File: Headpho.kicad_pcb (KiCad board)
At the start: 2 copper layers, 20 x 106.7 mm, 39 parts, among them IC1 NJM4556AD, IC2 NJM4556AD, J1 IN L, J2 IN R, J3 Eurorack_Power_10pin_Unshroud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, J4 LINE OUT L, J5 OUT LR, J6 LINE OUT R, U1 LME49720, U2 LME49720

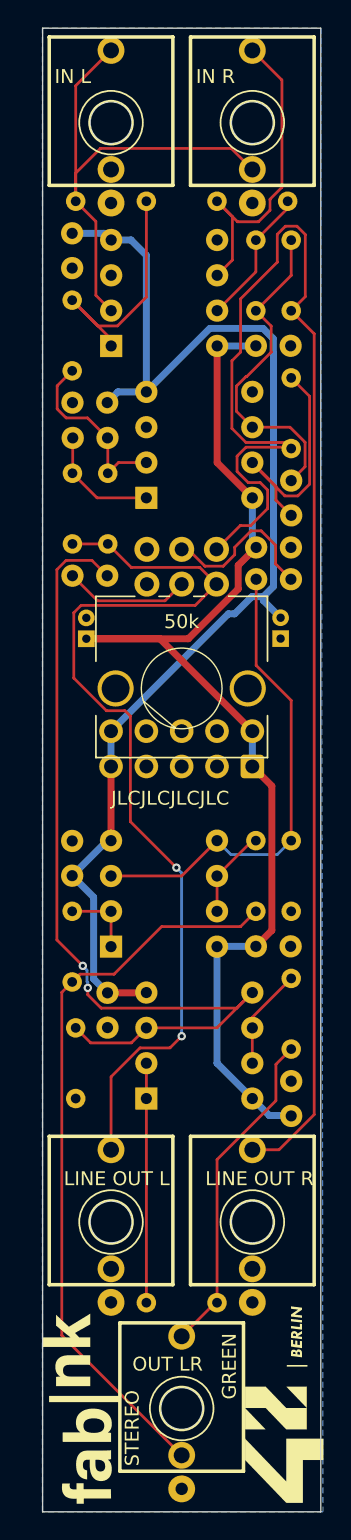
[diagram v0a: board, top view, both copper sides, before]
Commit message: added BuildNotes.md. Removed production folder
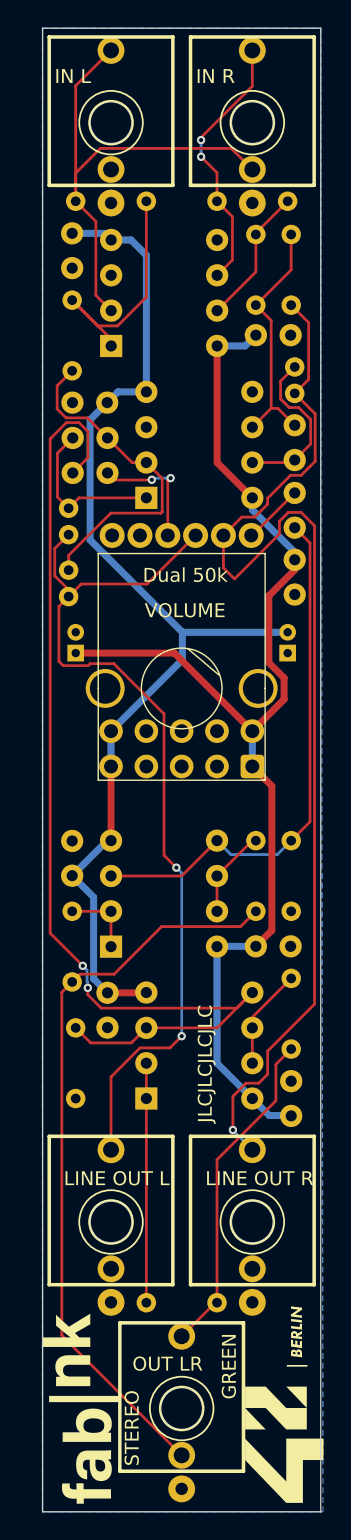
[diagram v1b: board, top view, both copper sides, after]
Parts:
- POT1: footprint PCM_4ms_Potentiometer:Potentiometer_Alps_RK09L_Double_Vertical -> Library:Dual_9mm_Potentiometer_50K_RK1114GH
- R5, R7, R8: footprint Resistor_THT:R_Axial_DIN0204_L3.6mm_D1.6mm_P5.08mm_Horizontal -> Resistor_THT:R_Axial_DIN0204_L3.6mm_D1.6mm_P1.90mm_Vertical
- moved C13 7.81 mm to (55.6, 82.8), turned to 180 degrees
- moved R5 7.51 mm to (52.8, 89.8)
- moved C14 6.21 mm to (69.1, 84.2), turned to -90 degrees
- moved C12 3.99 mm to (69.1, 79.4)
- moved C5 2.91 mm to (69.1, 89.0), turned to -90 degrees
- moved R7 2.53 mm to (52.8, 85.3)
- moved C1 1.28 mm to (53.3, 95.7)
- moved C2 1.16 mm to (68.6, 95.7)
- moved R8 0.83 mm to (69.1, 75.2)
- moved C3 0.77 mm to (66.3, 72.9)
- moved R4 0.40 mm to (66.3, 65.6)
- moved R6 0.40 mm to (68.8, 65.6)
- turned POT1 to 180 degrees
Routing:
- net Net-(J6-SIG): track 106.8 -> 82.4 mm, vias 0 -> 1
- net Net-(IC1-A_+INPUT): track 63.2 -> 75.3 mm
- net Net-(U2A--): track 13.3 -> 24.3 mm
- net -12V: track 90.1 -> 79.5 mm
- net Net-(POT1B-Center): track 11.9 -> 4.39 mm
- net Net-(C12-Pad2): track 18.6 -> 12.0 mm
- net Net-(U2B--): track 23.9 -> 18.3 mm
- net Net-(J2-SIG): track 23.7 -> 19.1 mm, vias 0 -> 2
- net Net-(IC2-A_+INPUT): track 34.7 -> 38.4 mm
- net Net-(C11-Pad2): track 8.59 -> 11.7 mm
- net Net-(J4-SIG): track 68.6 -> 65.6 mm
- net +12V: track 83.7 -> 85.0 mm
- net Net-(POT1A-Center): track 9.10 -> 9.01 mm, vias 0 -> 2

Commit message: v1.1 ready for final check
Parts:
- C1, C2: footprint Capacitor_THT:CP_Radial_D4.0mm_P1.50mm -> Capacitor_THT:CP_Radial_D4.0mm_P2.00mm
- IC1, U2: moved to F.Cu
- R1, R10, R2, R3, R4, R6, R9: footprint Resistor_THT:R_Axial_DIN0204_L3.6mm_D1.6mm_P5.08mm_Horizontal -> Resistor_THT:R_Axial_DIN0204_L3.6mm_D1.6mm_P1.90mm_Vertical
- R11, R12, R13, R14: value 1 -> 1Ω; footprint Resistor_THT:R_Axial_DIN0204_L3.6mm_D1.6mm_P5.08mm_Horizontal -> Resistor_THT:R_Axial_DIN0204_L3.6mm_D1.6mm_P1.90mm_Vertical
- moved R6 35.9 mm to (52.8, 97.8)
- moved R8 31.7 mm to (52.8, 102.3)
- moved C14 27.9 mm to (52.8, 106.9)
- moved C13 27.5 mm to (69.1, 106.8), turned to -90 degrees
- moved R7 23.4 mm to (69.1, 102.2)
- moved R9 20.2 mm to (65.3, 111.5), turned to 0 degrees
- moved R5 18.1 mm to (69.1, 97.6)
- moved R11 17.6 mm to (67.3, 127.2), turned to -90 degrees
- moved R1 16.7 mm to (53.1, 80.0)
- moved J3 16.4 mm to (66.0, 87.5)
- moved R12 16.4 mm to (54.6, 127.2)
- moved C11 16.2 mm to (64.6, 66.8)
- moved C6 15.7 mm to (68.3, 64.3), turned to -90 degrees
- moved C12 15.6 mm to (59.8, 66.8), turned to 180 degrees
- moved C2 15.3 mm to (53.3, 94.7)
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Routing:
- net Net-(IC1-A_+INPUT): track 75.3 -> 20.5 mm, vias 2 -> 0
- net Net-(R2-Pad2): track 9.96 -> 53.8 mm, vias 0 -> 6
- net Net-(C12-Pad2): track 12.0 -> 54.5 mm, vias 0 -> 6
- net Net-(C11-Pad2): track 11.7 -> 49.3 mm, vias 0 -> 2
- net GND: track 0.00 -> 26.4 mm, vias 0 -> 2
- net Net-(J2-SIG): track 19.1 -> 40.3 mm, vias 2 -> 0
- net Net-(U2B--): track 18.3 -> 38.9 mm
- net Net-(J6-SIG): track 82.4 -> 62.2 mm, vias 1 -> 3
- net Net-(IC2-A_+INPUT): track 38.4 -> 20.0 mm
- net Net-(J1-SIG): track 36.9 -> 52.8 mm
- net Net-(U2A--): track 24.3 -> 39.9 mm, vias 0 -> 1
- net -12V: track 79.5 -> 94.4 mm
- net Net-(IC1-A_-INPUT): track 17.2 -> 5.32 mm
- net Net-(J5-SIG): track 24.0 -> 33.3 mm
- net +12V: track 85.0 -> 76.6 mm
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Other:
- board text added: "V1.1"
- board text removed: "V1.0"
